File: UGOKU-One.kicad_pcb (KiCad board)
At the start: 2 copper layers, 63 x 63 mm, 56 parts, among them CN1 Conn_01x04, CN2 Conn_01x04, CN3 Conn_01x04, CN4 CAN, J2 Conn_02x03_Odd_Even, J3 Conn_01x02_Male, J4 PA10, J6 Conn_01x04, SW1 PF1, SW2 RESET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

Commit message: V0.4.4 2024-3-3 発注仕様
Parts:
- moved J4 0.29 mm to (2.54, 18.0)
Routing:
- net PWR: track 138.1 -> 139.4 mm
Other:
- board text added: "UGOKU One Ver0.4.4 UGOKU Lab 2024-3"
- board text removed: "UGOKU One Ver0.4.4 UGOKU Lab 2024-2"
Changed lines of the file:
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@@
         (effects (font (size 1.4 1.4) (thickness 0.15)))
     )
-    (fp_text value "PF1" (at 9.144 4.191) (layer "F.Fab")
+    (fp_text value "PF1" (at 9.144 4.191) (layer "F.Fab") hide
         (effects (font (size 1.4 1.4) (thickness 0.15)))
     )
@@
         (effects (font (size 1.4 1.4) (thickness 0.15)))
     )
-    (fp_text value "RESET" (at 9.144 4.191) (layer "F.Fab")
+    (fp_text value "RESET" (at 9.144 4.191) (layer "F.Fab") hide
         (effects (font (size 1.4 1.4) (thickness 0.15)))
     )
@@
         (effects (font (size 1 1) (thickness 0.15)))
     )
-    (fp_text value "Conn_01x02_Male" (at 1.25 4.4) (layer "F.Fab")
+    (fp_text value "Conn_01x02_Male" (at 1.25 4.4) (layer "F.Fab") hide
         (effects (font (size 1 1) (thickness 0.15)))
     )
@@
   )
   (footprint "Connector_PinHeader_2.54mm:PinHeader_1x03_P2.54mm_Vertical" (layer "F.Cu")
-    (at 2.25 18 -90)
+    (at 2.54 18 -90)
     (descr "Through hole straight pin header, 1x03, 2.54mm pitch, single row")
     (tags "Through hole pin header THT 1x03 2.54mm single row")
@@
     (property "ki_keywords" "connector")
     (attr through_hole)
-    (fp_text reference "J4" (at -2.45 0.75 180) (layer "F.SilkS") hide
+    (fp_text reference "J4" (at -2.45 0.75) (layer "F.SilkS") hide
         (effects (font (size 1 1) (thickness 0.15)))
     )
@@
     (effects (font (size 1.1 1.1) (thickness 0.18)) (justify mirror))
   )
-  (gr_text "UGOKU One Ver0.4.4 UGOKU Lab 2024-2" (at 30.3 0 90) (layer "B.SilkS")
+  (gr_text "UGOKU One Ver0.4.4 UGOKU Lab 2024-3" (at 30.3 0 90) (layer "B.SilkS")
     (effects (font (size 1 1) (thickness 0.15)) (justify mirror))
   )
@@
     (effects (font (size 1 1) (thickness 0.15)))
   )
-  (gr_text "GND" (at 8.3 -0.7 90) (layer "F.SilkS")
-    (effects (font (size 0.8 0.8) (thickness 0.12) bold))
-  )
   (gr_text "6-32V" (at 1.8 15.3) (layer "F.SilkS")
     (effects (font (size 1 1) (thickness 0.15)))
@@
     (effects (font (size 0.6 0.6) (thickness 0.08)))
   )
-  (gr_text "GND\n" (at 6.3 2) (layer "F.SilkS")
+  (gr_text "GND\n" (at 6.3 2.3) (layer "F.SilkS")
     (effects (font (size 0.6 0.6) (thickness 0.12) bold))
   )
@@
   (segment (start -24.406 7.5) (end -23.256 6.35) (width 1.3) (layer "F.Cu") (net 4))
   (segment (start -21.7 20.3) (end -22.5 19.5) (width 1.3) (layer "B.Cu") (net 4))
-  (segment (start 1 22.525) (end -0.0488 21.4762) (width 1.3) (layer "B.Cu") (net 4))
   (segment (start 17.0541 22.0041) (end 17.55 22.5) (width 1.3) (layer "B.Cu") (net 4))
   (segment (start -19.025 20.3) (end -21.7 20.3) (width 1.3) (layer "B.Cu") (net 4))
@@
   (segment (start 17.55 21.775) (end 19.825 19.5) (width 1.3) (layer "B.Cu") (net 4))
   (segment (start -17.8488 21.4762) (end -16.5262 21.4762) (width 1.3) (layer "B.Cu") (net 4))
+  (segment (start 0 18) (end 0 5.2) (width 1.3) (layer "B.Cu") (net 4))
   (segment (start -18.1875 21.1375) (end -17.8488 21.4762) (width 1.3) (layer "B.Cu") (net 4))
-  (segment (start -0.0488 21.4762) (end -0.29 21.235) (width 1.3) (layer "B.Cu") (net 4))
+  (segment (start 0 5.2) (end 1.7 3.5) (width 1.3) (layer "B.Cu") (net 4))
   (segment (start 1 23.5) (end 1 22.525) (width 1.3) (layer "B.Cu") (net 4))
   (segment (start 17.55 22.5) (end 17.55 21.775) (width 1.3) (layer "B.Cu") (net 4))
+  (segment (start -0.0488 21.4762) (end 1 22.525) (width 1.3) (layer "B.Cu") (net 4))
   (segment (start -17.55 22.5) (end -16.5262 21.4762) (width 1.3) (layer "B.Cu") (net 4))
   (segment (start -18.1875 21.1375) (end -17.8488 21.4762) (width 1.3) (layer "B.Cu") (net 4))
@@
   (segment (start -18.1875 21.1375) (end -19.025 20.3) (width 1.3) (layer "B.Cu") (net 4))
   (segment (start 2.5 26) (end 6.4959 22.0041) (width 1.3) (layer "B.Cu") (net 4))
-  (segment (start -0.29 5.49) (end 1.7 3.5) (width 1.3) (layer "B.Cu") (net 4))
-  (segment (start 6.4959 22.0041) (end 17.0541 22.0041) (width 1.3) (layer "B.Cu") (net 4))
-  (segment (start -0.29 21.235) (end -0.29 18) (width 1.3) (layer "B.Cu") (net 4))
-  (segment (start -0.29 18) (end -0.29 5.49) (width 1.3) (layer "B.Cu") (net 4))
+  (segment (start 1 22.525) (end 0 21.525) (width 1.3) (layer "B.Cu") (net 4))
+  (segment (start 0 21.525) (end 0 18) (width 1.3) (layer "B.Cu") (net 4))
   (segment (start -16.5262 21.4762) (end -0.0488 21.4762) (width 1.3) (layer "B.Cu") (net 4))
+  (segment (start 6.4959 22.0041) (end 17.0541 22.0041) (width 1.3) (layer "B.Cu") (net 4))
   (segment (start -17.8488 21.4762) (end -17.55 21.775) (width 1.3) (layer "B.Cu") (net 4))
   (segment (start 14.425 -17.25) (end 13.6 -16.425) (width 0.25) (layer "F.Cu") (net 5))
@@
   (segment (start -28.45 0.05) (end -28.45 18.6592) (width 1.3) (layer "F.Cu") (net 37))
   (segment (start -26.644 -0.5) (end -27.9 -0.5) (width 1.3) (layer "F.Cu") (net 37))
-  (segment (start 14.5602 20.1808) (end 21.0165 13.7245) (width 0.25) (layer "F.Cu") (net 38))
-  (segment (start -1.6852 20.1808) (end 14.5602 20.1808) (width 0.25) (layer "F.Cu") (net 38))
+  (segment (start 14.591 20.15) (end 21.0165 13.7245) (width 0.25) (layer "F.Cu") (net 38))
+  (segment (start -1.4 20.15) (end 14.591 20.15) (width 0.25) (layer "F.Cu") (net 38))
   (via (at 21.0165 13.7245) (size 0.6) (drill 0.3) (layers "F.Cu" "B.Cu") (net 38))
-  (via (at -1.6852 20.1808) (size 0.6) (drill 0.3) (layers "F.Cu" "B.Cu") (net 38))
+  (via (at -1.4 20.15) (size 0.6) (drill 0.3) (layers "F.Cu" "B.Cu") (net 38))
   (segment (start 26.0709 6.5909) (end 24.95 5.47) (width 0.25) (layer "B.Cu") (net 38))
   (segment (start 21.0165 13.7245) (end 24.1901 13.7245) (width 0.25) (layer "B.Cu") (net 38))
-  (segment (start -2.88 14.925) (end -1.6307 16.1743) (width 0.25) (layer "B.Cu") (net 38))
+  (segment (start -1.365 16.44) (end -1.365 20.115) (width 0.25) (layer "B.Cu") (net 38))
   (segment (start 26.0709 11.8437) (end 26.0709 6.5909) (width 0.25) (layer "B.Cu") (net 38))
+  (segment (start -2.88 14.925) (end -1.365 16.44) (width 0.25) (layer "B.Cu") (net 38))
   (segment (start 24.1901 13.7245) (end 26.0709 11.8437) (width 0.25) (layer "B.Cu") (net 38))
-  (segment (start -1.6307 20.1263) (end -1.6852 20.1808) (width 0.25) (layer "B.Cu") (net 38))
-  (segment (start -1.6307 16.1743) (end -1.6307 20.1263) (width 0.25) (layer "B.Cu") (net 38))
+  (segment (start -1.365 20.115) (end -1.4 20.15) (width 0.25) (layer "B.Cu") (net 38))
   (segment (start -20.1847 -12.5695) (end -19.2812 -11.666) (width 0.25) (layer "F.Cu") (net 40))
   (segment (start -22.7 -12.5695) (end -20.1847 -12.5695) (width 0.25) (layer "F.Cu") (net 40))
@@
   (segment (start 14.59912 19.4105) (end 16.425 17.58462) (width 0.25) (layer "F.Cu") (net 52))
   (segment (start 16.425 17.58462) (end 16.425 11.41538) (width 0.25) (layer "F.Cu") (net 52))
-  (segment (start 2.25 12.75) (end 2.42 12.58) (width 1.3) (layer "B.Cu") (net 54))
-  (segment (start 2.25 18) (end 2.25 12.75) (width 1.3) (layer "B.Cu") (net 54))
-  (segment (start 2.25 18) (end 2.42 17.83) (width 1.3) (layer "B.Cu") (net 54))
-  (segment (start 2.42 12.58) (end 2.42 7.75) (width 1.3) (layer "B.Cu") (net 54))
+  (segment (start 2.1445 17.825) (end 2.3195 18) (width 1.75) (layer "B.Cu") (net 54))
+  (segment (start 2.42 7.75) (end 2.1445 8.0255) (width 1.75) (layer "B.Cu") (net 54))
+  (segment (start 2.1445 8.0255) (end 2.1445 17.825) (width 1.75) (layer "B.Cu") (net 54))
   (segment (start 10.25 -21.725) (end 10.25 -19.825) (width 0.25) (layer "F.Cu") (net 55))
   (segment (start -0.5576 -6.0047) (end -0.5576 -5.826) (width 0.25) (layer "F.Cu") (net 56))
@@
   (segment (start -0.25 -11.05) (end 0.5 -11.05) (width 0.25) (layer "B.Cu") (net 58))
   (segment (start -0.575 -15.79) (end -0.575 -11.375) (width 0.25) (layer "B.Cu") (net 58))
-  (segment (start -2.83 18) (end -1.111 16.281) (width 0.4) (layer "F.Cu") (net 87))
-  (segment (start -1.111 15.0292) (end -1.111 15.0291) (width 0.4) (layer "F.Cu") (net 87))
   (segment (start 16.179 -9.2028) (end 17.2528 -9.2028) (width 0.4) (layer "F.Cu") (net 87))
   (segment (start -4.4341 11.138438) (end -6.489038 9.0835) (width 0.4) (layer "F.Cu") (net 87))
@@
   (segment (start 18.25 -10.2) (end 18.25 -10.8104) (width 0.4) (layer "F.Cu") (net 87))
   (segment (start 7.5 7.75) (end 7.5 3.8) (width 1.3) (layer "F.Cu") (net 87))
-  (segment (start -3.3139 13.655) (end -4.4341 12.5348) (width 0.4) (layer "F.Cu") (net 87))
+  (segment (start -1.111 16.571) (end -1.111 15.0291) (width 0.4) (layer "F.Cu") (net 87))
+  (segment (start -2.54 18) (end -1.111 16.571) (width 0.4) (layer "F.Cu") (net 87))
   (segment (start 20.5781 -13.1385) (end 21.2146 -13.1385) (width 0.4) (layer "F.Cu") (net 87))
+  (segment (start -3.3139 13.655) (end -4.4341 12.5348) (width 0.4) (layer "F.Cu") (net 87))
   (segment (start -4.4341 11.138438) (end 1.961562 11.138438) (width 0.4) (layer "F.Cu") (net 87))
-  (segment (start 1.961562 11.138438) (end 2.65 10.45) (width 0.4) (layer "F.Cu") (net 87))
   (segment (start -4.4341 12.5348) (end -4.4341 11.138438) (width 0.4) (layer "F.Cu") (net 87))
+  (segment (start 1.961562 11.138438) (end 2.65 10.45) (width 0.4) (layer "F.Cu") (net 87))
+  (segment (start -2.4852 13.655) (end -3.3139 13.655) (width 0.4) (layer "F.Cu") (net 87))
   (segment (start 4.8 10.45) (end 2.65 10.45) (width 0.4) (layer "F.Cu") (net 87))
   (segment (start 13.615 -12.65) (end 13.615 -11.9) (width 0.4) (layer "F.Cu") (net 87))
@@
   (segment (start 18.25 -11.4207) (end 16.4207 -13.25) (width 0.4) (layer "F.Cu") (net 87))
   (segment (start 16.4207 -13.25) (end 14.215 -13.25) (width 0.4) (layer "F.Cu") (net 87))
-  (segment (start -2.4852 13.655) (end -3.3139 13.655) (width 0.4) (layer "F.Cu") (net 87))
-  (segment (start -1.111 16.281) (end -1.111 15.0292) (width 0.4) (layer "F.Cu") (net 87))
   (segment (start 18.25 -10.8104) (end 18.25 -11.4207) (width 0.4) (layer "F.Cu") (net 87))
   (segment (start 21.2146 -13.1385) (end 23.7772 -15.7011) (width 0.4) (layer "F.Cu") (net 87))

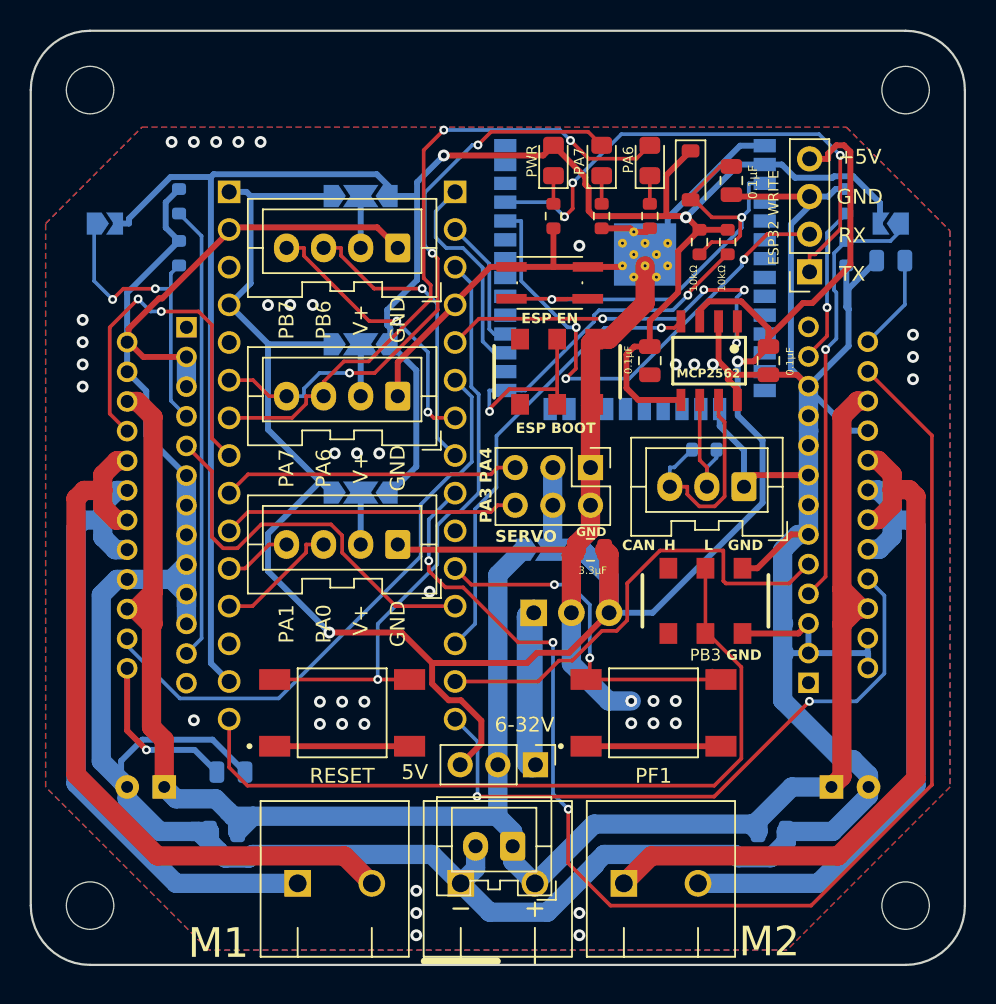
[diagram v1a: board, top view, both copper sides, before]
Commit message: Modify ESP32 position
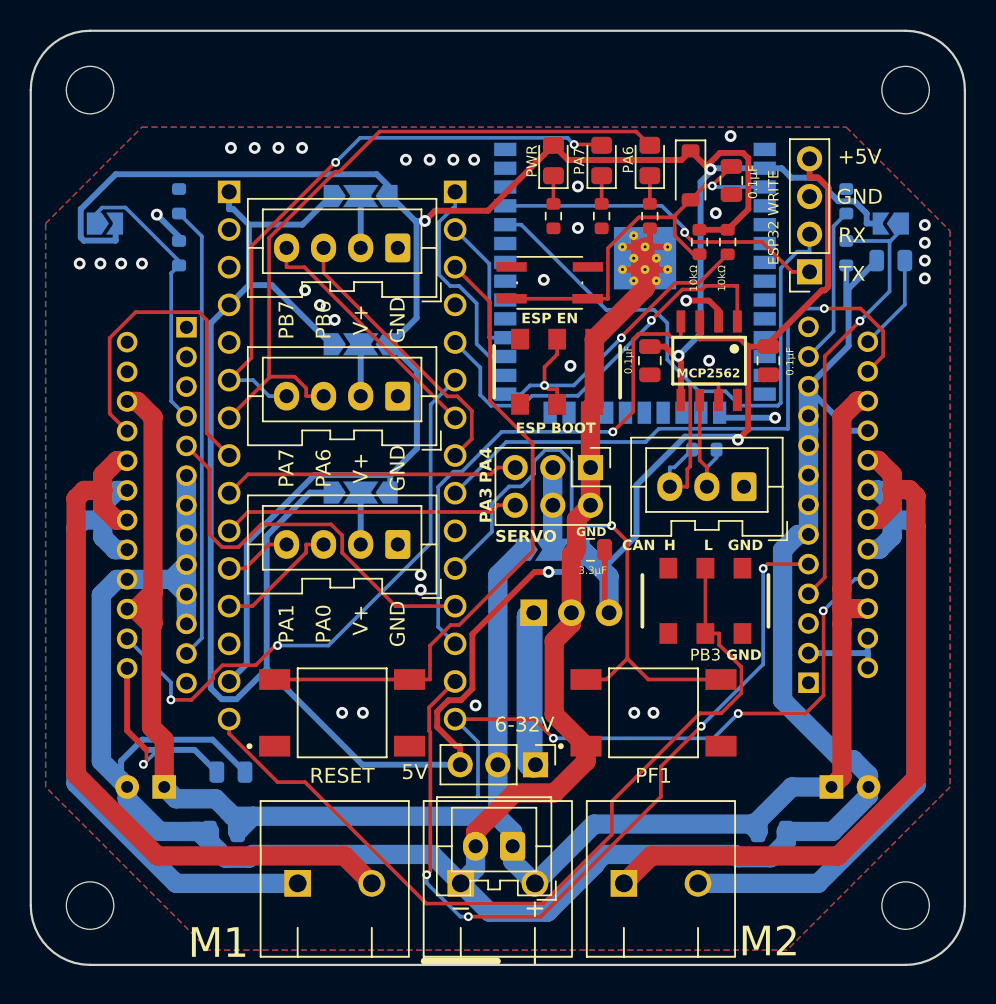
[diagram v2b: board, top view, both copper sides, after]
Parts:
- moved U7 0.25 mm to (9.25, -15.2)
- renumbered REF** to MH1, REF** to MH2, REF** to MH3, REF** to MH4
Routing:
- net GND: track 390.6 -> 233.5 mm, vias 41 -> 36
- net Net-(U2A-PB1): track 90.4 -> 41.9 mm, vias 3 -> 1
- net Net-(U2A-PB5): track 31.6 -> 56.0 mm, vias 0 -> 4
- net +5V: track 141.7 -> 158.5 mm
- net Net-(U2A-PF1): track 24.9 -> 39.2 mm, vias 2 -> 1
- net Net-(J6-Pin_1): track 35.8 -> 22.6 mm, vias 3 -> 1
- net Net-(D1-A): track 37.4 -> 27.6 mm, vias 2 -> 1
- net +3V3: track 145.8 -> 138.7 mm, vias 2 -> 3
- net Net-(U7-IO0): track 31.3 -> 24.4 mm
- net Net-(U2A-PA11): track 30.9 -> 35.7 mm
- net Net-(U2B-PB3): track 53.0 -> 57.4 mm
- net PWR: track 139.4 -> 135.4 mm
- net Net-(J6-Pin_2): track 34.6 -> 37.8 mm, vias 3 -> 0
- net Net-(U2A-NRST_1): track 40.8 -> 43.7 mm, vias 1 -> 0
- net Net-(U5-VREG): track 11.4 -> 13.8 mm
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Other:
- board text added: "SERVO POWER SOURCE"
- board text added: "UGOKU One Ver0.4.5 UGOKU Lab 2024-4"
- board text removed: "UGOKU One Ver0.4.4 UGOKU Lab 2024-3"
